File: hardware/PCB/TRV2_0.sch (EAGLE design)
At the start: 54 parts, among them IC1 TMP112, IC2 SHT21, IC4 CNY70, IC5 ATMEGA8-AU, Q1 FC-12M

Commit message: Schematic done
NOTE: INT on light sensor not found anywhere else on schematic.
NOTE: Comms connector differs from Standard.
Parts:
- removed C13: 10uF 6V, resistor:CPOL-EUSMCB
- added C18: 10uF 6V, resistor:CPOL-EUSMCB
- added IC3: APDS-9300-020, APDS-9300-020:APDS-9300-020
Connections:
- new net INT: IC3.INT
- net GND: now also C18.-, IC3.ADDR_SEL, IC3.GND; no longer C13.-
- net RFVCC: now also C18.+; no longer C13.+
- net SCL: now also IC1.SCL, IC3.SCL, SV1.9
- net SDA: now also IC1.SDA, IC3.SDA
- net SPI_MISO: now also SV1.1
- net SPI_SCLK: now also SV1.3; no longer IC5.DIGITAL_13(LED)
- net VCC: now also C1.1, C2.1, IC1.V+, IC3.VCC
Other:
- moved on the sheet: C1, C10, C11, C12, C16, C17, C2, C3, C4, C5, C6, C7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

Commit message: double checked schematic
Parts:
- renumbered SV1 to J1
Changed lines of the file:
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@@
 <part name="GND18" library="supply1" deviceset="GND" device=""/>
 <part name="GND19" library="supply1" deviceset="GND" device=""/>
-<part name="SV1" library="con-lstb" deviceset="MA07-2" device=""/>
+<part name="J1" library="con-lstb" deviceset="MA07-2" device=""/>
 <part name="GND20" library="supply1" deviceset="GND" device=""/>
 <part name="C7" library="rcl" deviceset="C-EU" device="C0603" value="100N"/>
@@
 <instance part="GND18" gate="1" x="322.58" y="203.2"/>
 <instance part="GND19" gate="1" x="340.36" y="203.2"/>
-<instance part="SV1" gate="G$1" x="330.2" y="137.16" rot="R180"/>
+<instance part="J1" gate="G$1" x="330.2" y="137.16" rot="R180"/>
 <instance part="GND20" gate="1" x="345.44" y="139.7" rot="R90"/>
 <instance part="C7" gate="G$1" x="365.76" y="139.7"/>
@@
 </segment>
 <segment>
-<pinref part="SV1" gate="G$1" pin="2"/>
+<pinref part="J1" gate="G$1" pin="2"/>
 <wire x1="337.82" y1="144.78" x2="340.36" y2="144.78" width="0.1524" layer="91"/>
 <label x="337.82" y="144.78" size="1.778" layer="95"/>
@@
 </segment>
 <segment>
-<pinref part="SV1" gate="G$1" pin="6"/>
+<pinref part="J1" gate="G$1" pin="6"/>
 <pinref part="GND20" gate="1" pin="GND"/>
 <wire x1="342.9" y1="139.7" x2="337.82" y2="139.7" width="0.1524" layer="91"/>
@@
 <wire x1="322.58" y1="134.62" x2="320.04" y2="134.62" width="0.1524" layer="91"/>
 <label x="312.42" y="134.62" size="1.778" layer="95"/>
-<pinref part="SV1" gate="G$1" pin="9"/>
+<pinref part="J1" gate="G$1" pin="9"/>
 </segment>
 <segment>
@@
 </segment>
 <segment>
-<pinref part="SV1" gate="G$1" pin="10"/>
+<pinref part="J1" gate="G$1" pin="10"/>
 <wire x1="337.82" y1="134.62" x2="340.36" y2="134.62" width="0.1524" layer="91"/>
 <label x="340.36" y="134.62" size="1.778" layer="95"/>
@@
 </segment>
 <segment>
-<pinref part="SV1" gate="G$1" pin="14"/>
+<pinref part="J1" gate="G$1" pin="14"/>
 <wire x1="337.82" y1="129.54" x2="340.36" y2="129.54" width="0.1524" layer="91"/>
 <label x="340.36" y="129.54" size="1.778" layer="95"/>
@@
 </segment>
 <segment>
-<pinref part="SV1" gate="G$1" pin="4"/>
+<pinref part="J1" gate="G$1" pin="4"/>
 <wire x1="337.82" y1="142.24" x2="340.36" y2="142.24" width="0.1524" layer="91"/>
 <label x="337.82" y="142.24" size="1.778" layer="95"/>
@@
 <wire x1="322.58" y1="144.78" x2="320.04" y2="144.78" width="0.1524" layer="91"/>
 <label x="312.42" y="144.78" size="1.778" layer="95"/>
-<pinref part="SV1" gate="G$1" pin="1"/>
+<pinref part="J1" gate="G$1" pin="1"/>
 </segment>
 <segment>
@@
 <wire x1="322.58" y1="142.24" x2="320.04" y2="142.24" width="0.1524" layer="91"/>
 <label x="312.42" y="142.24" size="1.778" layer="95"/>
-<pinref part="SV1" gate="G$1" pin="3"/>
+<pinref part="J1" gate="G$1" pin="3"/>
 </segment>
 <segment>
@@
 <wire x1="210.82" y1="25.4" x2="203.2" y2="25.4" width="0.1524" layer="91"/>
 <label x="198.12" y="25.4" size="1.778" layer="95"/>
+</segment>
+<segment>
+<wire x1="190.5" y1="48.26" x2="177.8" y2="48.26" width="0.1524" layer="91"/>
+<label x="180.34" y="48.26" size="1.778" layer="95"/>
 </segment>
 </net>
@@
 <net name="RESET" class="0">
 <segment>
-<pinref part="SV1" gate="G$1" pin="5"/>
+<pinref part="J1" gate="G$1" pin="5"/>
 <wire x1="322.58" y1="139.7" x2="320.04" y2="139.7" width="0.1524" layer="91"/>
 <label x="312.42" y="139.7" size="1.778" layer="95"/>
@@
 <net name="BOILER" class="0">
 <segment>
-<pinref part="SV1" gate="G$1" pin="7"/>
+<pinref part="J1" gate="G$1" pin="7"/>
 <wire x1="322.58" y1="137.16" x2="320.04" y2="137.16" width="0.1524" layer="91"/>
 <label x="312.42" y="137.16" size="1.778" layer="95"/>
@@
 <net name="RXD0B" class="0">
 <segment>
-<pinref part="SV1" gate="G$1" pin="11"/>
+<pinref part="J1" gate="G$1" pin="11"/>
 <wire x1="322.58" y1="132.08" x2="320.04" y2="132.08" width="0.1524" layer="91"/>
 <label x="312.42" y="132.08" size="1.778" layer="95"/>
@@
 <net name="N$2" class="0">
 <segment>
-<pinref part="SV1" gate="G$1" pin="8"/>
+<pinref part="J1" gate="G$1" pin="8"/>
 <wire x1="337.82" y1="137.16" x2="340.36" y2="137.16" width="0.1524" layer="91"/>
 </segment>
@@
 <net name="TXD0B" class="0">
 <segment>
-<pinref part="SV1" gate="G$1" pin="12"/>
+<pinref part="J1" gate="G$1" pin="12"/>
 <wire x1="337.82" y1="132.08" x2="340.36" y2="132.08" width="0.1524" layer="91"/>
 <label x="340.36" y="132.08" size="1.778" layer="95"/>

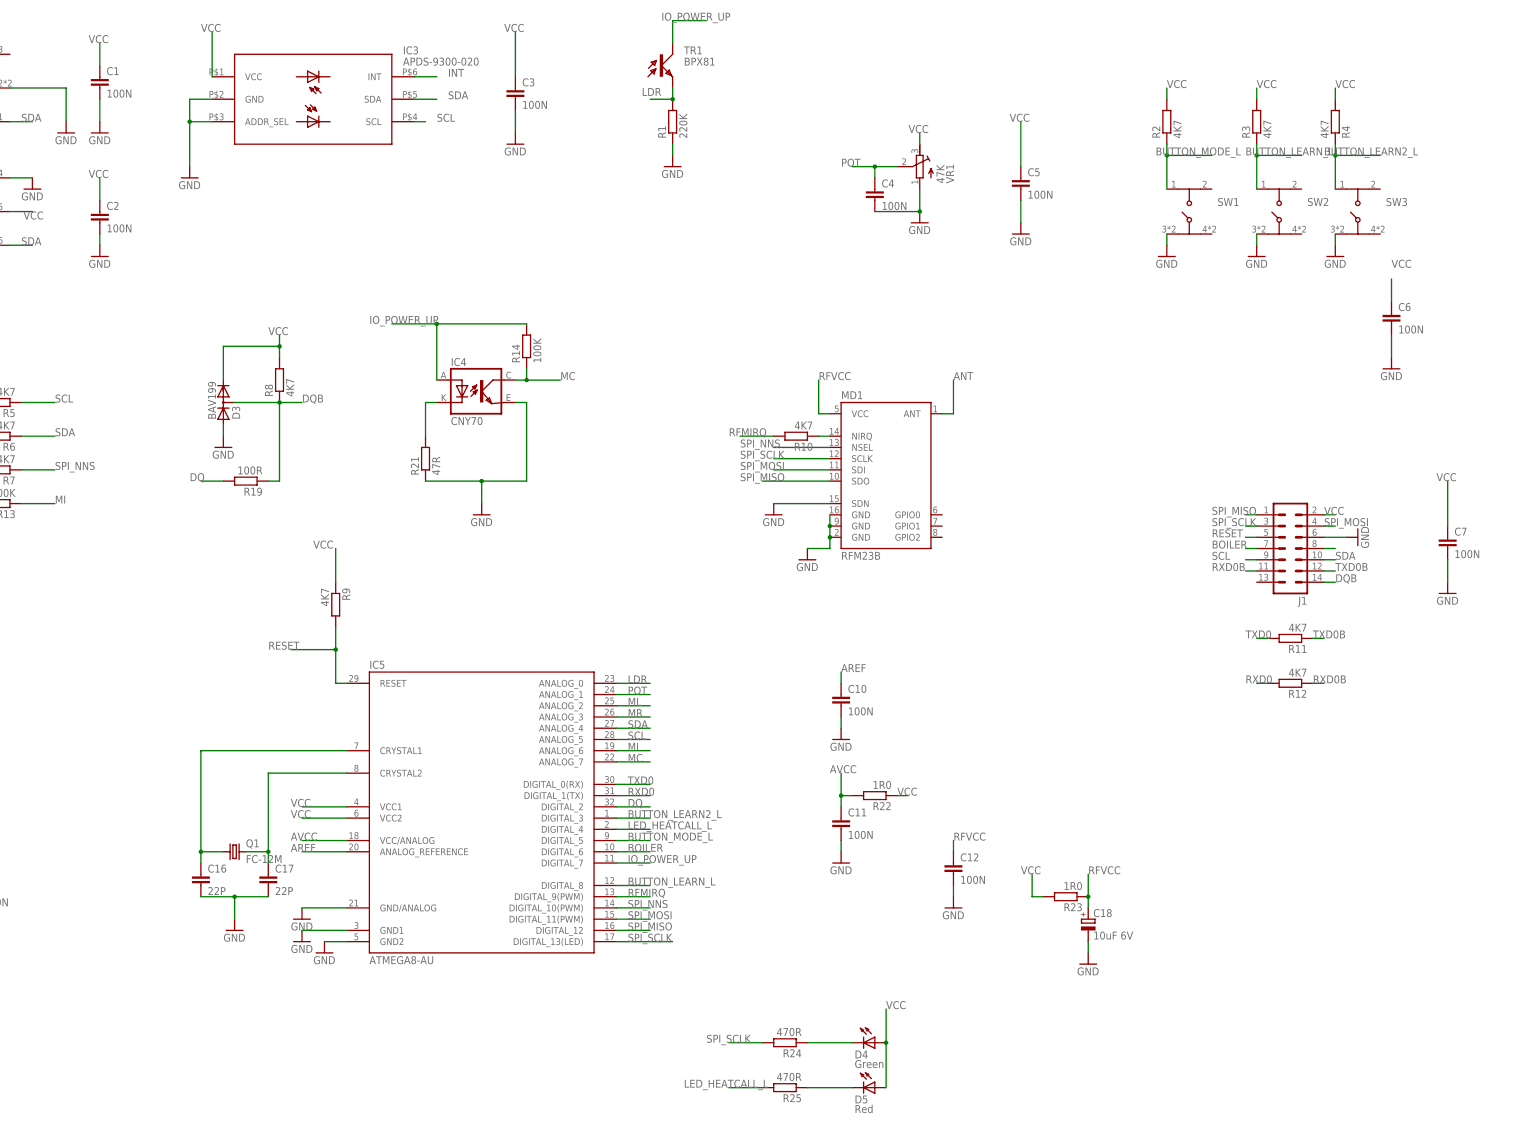
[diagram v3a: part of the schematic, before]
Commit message: added motor header
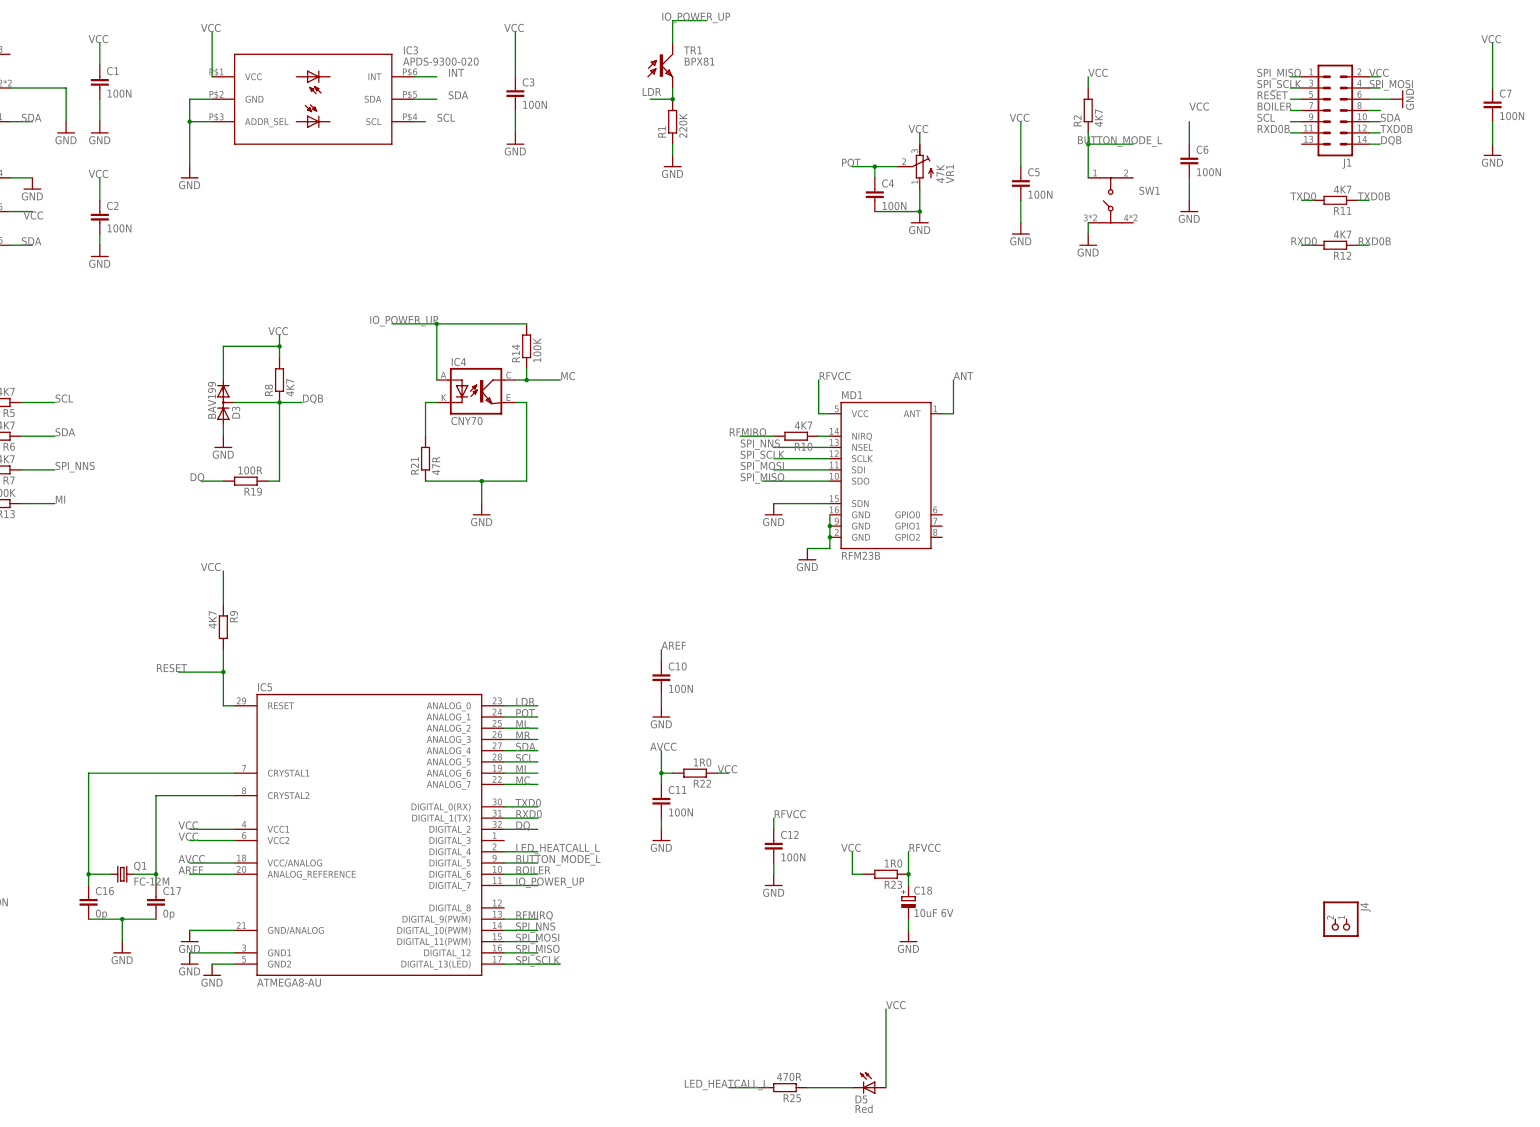
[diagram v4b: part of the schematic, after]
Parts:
- removed D4: Green, adafruit:LED3MM
- removed R24: 470R, resistor:R-EU_R0603
- removed R3, R4: 4K7, resistor:R-EU_R0603
- removed SW2, SW3: (no value), EAGLE-TACT_SWITCHES-rev16e:434331013822
- added J4: (no value), pinhead:PINHD-1X2
- C16, C17: value 22P -> 0p
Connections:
- removed net BUTTON_LEARN2_L: IC5.DIGITAL_3, R4.1, SW3.1
- removed net BUTTON_LEARN_L: IC5.DIGITAL_8, R3.1, SW2.1
- removed net N$6: D4.C, R24.1
- net GND: no longer SW2.3, SW3.3
- net SPI_SCLK: now also IC5.DIGITAL_13(LED); no longer R24.2
- net VCC: no longer D4.A, R3.2, R4.2
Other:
- moved on the sheet: C10, C11, C12, C16, C17, C18, C6, C7, IC5, J1, Q1, R11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

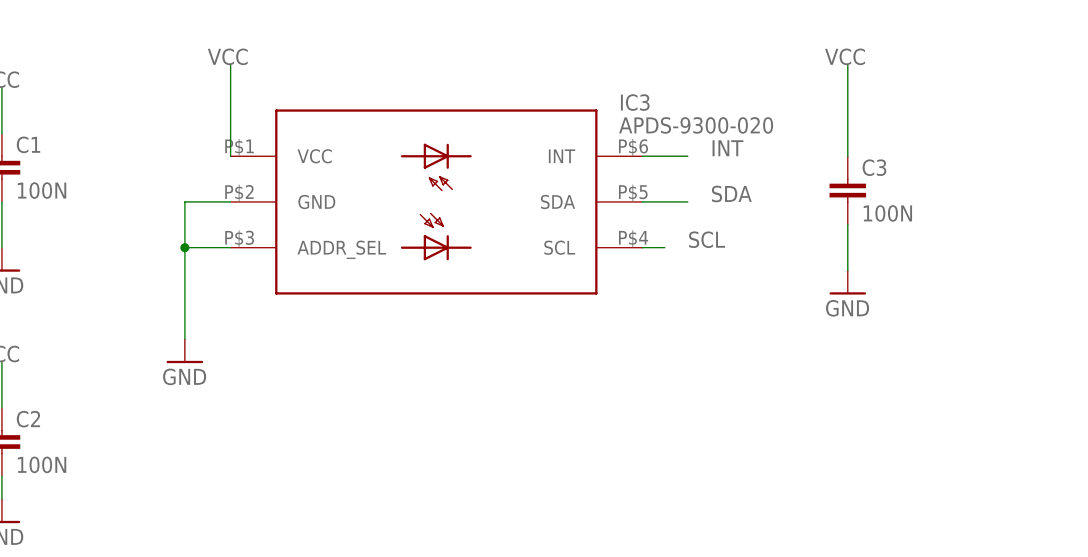
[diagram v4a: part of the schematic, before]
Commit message: cleaned up
Issues this far

>>>- We don't want the RFM23B on this model (Damon, do we want to keep
the footprint?)
>>>- We want TR1 and D5 to be SMD devices with the 'active' side on the
top edge of the board.
>>>-Why does comms connector not use our standard 100%? pin8 was not
labeled at all and one more had a different name
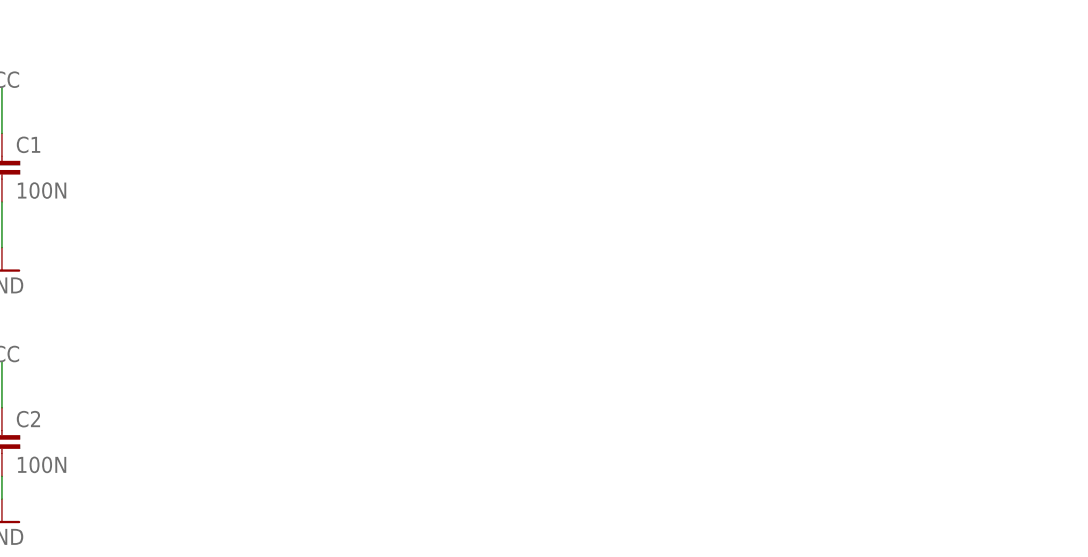
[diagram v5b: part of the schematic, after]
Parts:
- removed C3: 100N, rcl:C-EUC0603
- removed IC3: APDS-9300-020, APDS-9300-020:APDS-9300-020
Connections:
- removed net INT: IC3.INT
- net GND: no longer C3.2, IC3.ADDR_SEL, IC3.GND
- net SCL: no longer IC3.SCL
- net SDA: no longer IC3.SDA
- net VCC: no longer C3.1, IC3.VCC
